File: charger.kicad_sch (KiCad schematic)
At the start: 5 parts, among them J1 Barrel_Jack_Switch, U2 DSIC08LSGET_C3293158

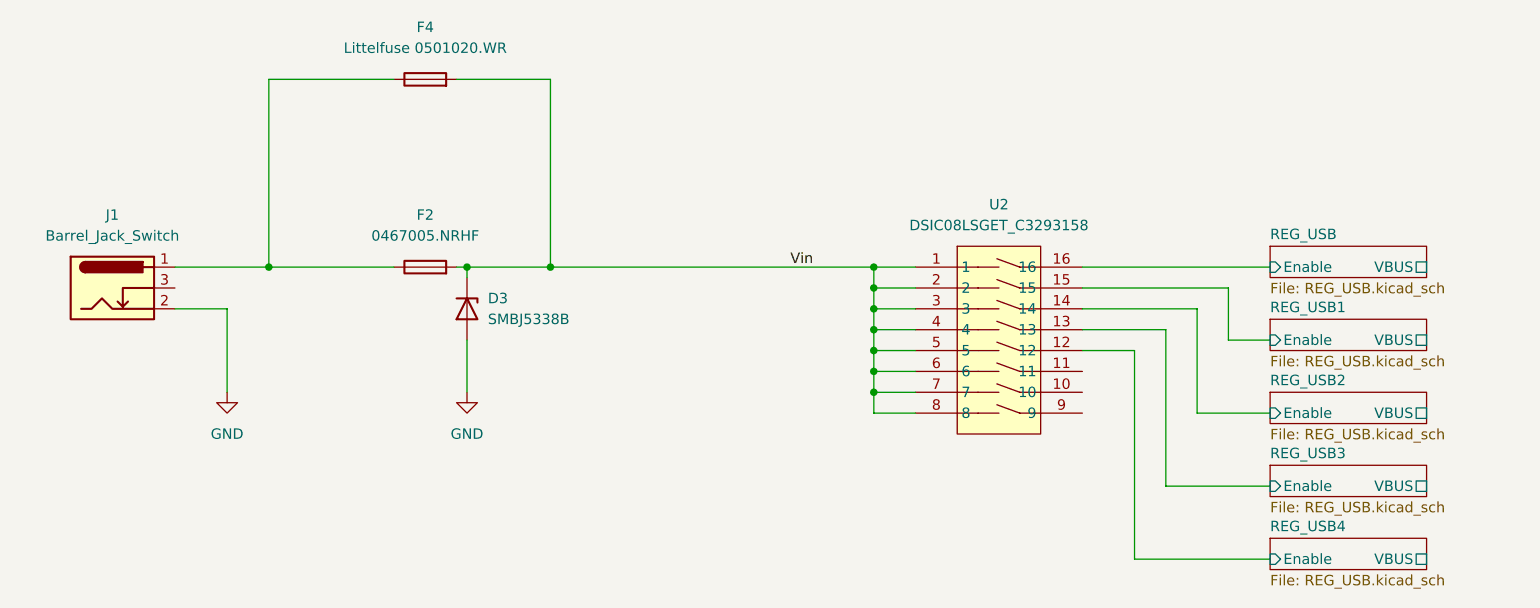
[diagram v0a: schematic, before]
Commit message: finished getting footprints and started layout
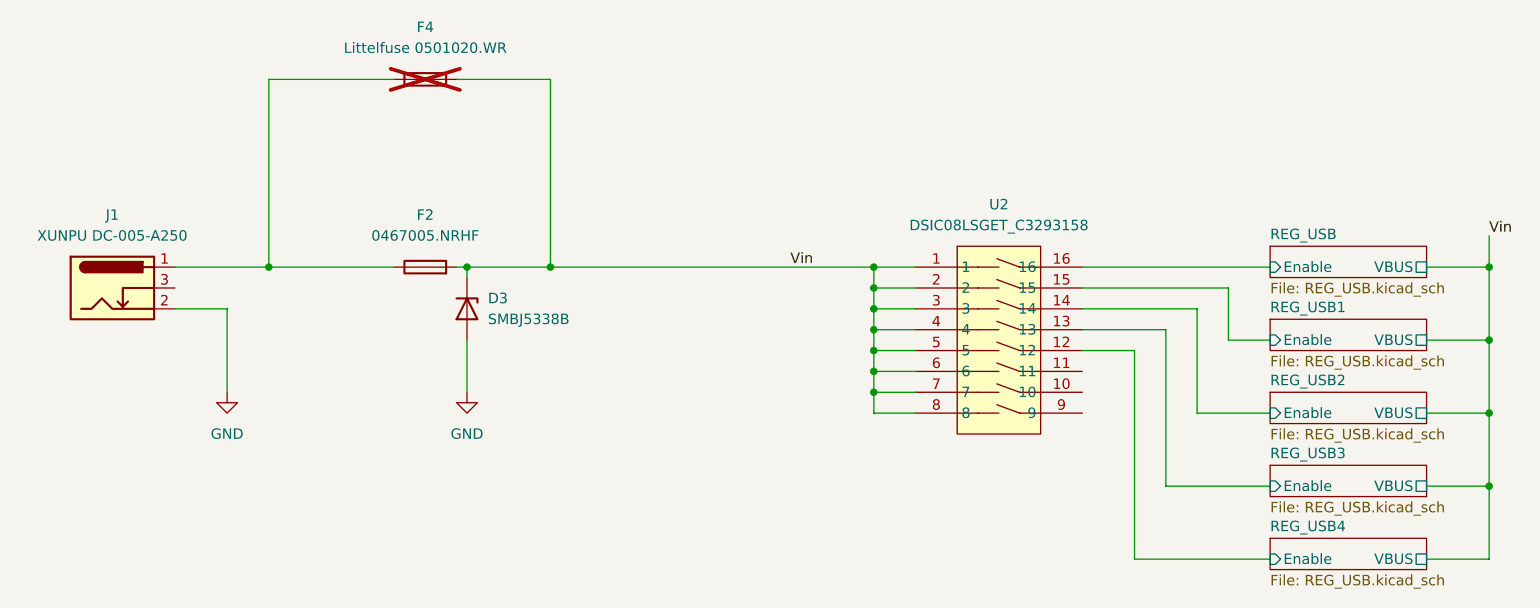
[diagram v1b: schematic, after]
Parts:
- F4: now not fitted
- J1: value Barrel_Jack_Switch -> XUNPU DC-005-A250; footprint (none) -> easyeda2kicad:DC-IN-TH_DC-005-A250
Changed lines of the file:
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@@
+	)
+	(junction
+		(at 204.47 83.82)
+		(diameter 0)
+		(color 0 0 0 0)
 	)
 	(junction
@@
 	)
 	(junction
+		(at 204.47 66.04)
+		(diameter 0)
+		(color 0 0 0 0)
+	)
+	(junction
+		(at 204.47 92.71)
+		(diameter 0)
+		(color 0 0 0 0)
+	)
+	(junction
+		(at 204.47 74.93)
+		(diameter 0)
+		(color 0 0 0 0)
+	)
+	(junction
 		(at 90.17 66.04)
 		(diameter 0)
@@
 	(wire
 		(pts
+			(xy 204.47 66.04) (xy 204.47 74.93)
+		)
+		(stroke
+			(width 0)
+			(type default)
+		)
+	)
+	(wire
+		(pts
 			(xy 44.45 71.12) (xy 50.8 71.12)
 		)
@@
 	(wire
 		(pts
+			(xy 204.47 83.82) (xy 204.47 92.71)
+		)
+		(stroke
+			(width 0)
+			(type default)
+		)
+	)
+	(wire
+		(pts
 			(xy 129.54 71.12) (xy 129.54 68.58)
 		)
@@
 	(wire
 		(pts
+			(xy 204.47 74.93) (xy 204.47 83.82)
+		)
+		(stroke
+			(width 0)
+			(type default)
+		)
+	)
+	(wire
+		(pts
 			(xy 129.54 68.58) (xy 134.62 68.58)
 		)
@@
 	(wire
 		(pts
+			(xy 196.85 83.82) (xy 204.47 83.82)
+		)
+		(stroke
+			(width 0)
+			(type default)
+		)
+	)
+	(wire
+		(pts
 			(xy 44.45 66.04) (xy 55.88 66.04)
 		)
@@
 	(wire
 		(pts
+			(xy 204.47 62.23) (xy 204.47 66.04)
+		)
+		(stroke
+			(width 0)
+			(type default)
+		)
+	)
+	(wire
+		(pts
 			(xy 80.01 66.04) (xy 80.01 67.31)
 		)
@@
 	(wire
 		(pts
+			(xy 196.85 92.71) (xy 204.47 92.71)
+		)
+		(stroke
+			(width 0)
+			(type default)
+		)
+	)
+	(wire
+		(pts
 			(xy 161.29 101.6) (xy 177.8 101.6)
 		)
@@
 	(wire
 		(pts
+			(xy 196.85 74.93) (xy 204.47 74.93)
+		)
+		(stroke
+			(width 0)
+			(type default)
+		)
+	)
+	(wire
+		(pts
 			(xy 129.54 66.04) (xy 134.62 66.04)
 		)
@@
 	(wire
 		(pts
+			(xy 204.47 92.71) (xy 204.47 101.6)
+		)
+		(stroke
+			(width 0)
+			(type default)
+		)
+	)
+	(wire
+		(pts
 			(xy 80.01 66.04) (xy 90.17 66.04)
 		)
@@
 	(wire
 		(pts
+			(xy 196.85 101.6) (xy 204.47 101.6)
+		)
+		(stroke
+			(width 0)
+			(type default)
+		)
+	)
+	(wire
+		(pts
 			(xy 129.54 76.2) (xy 134.62 76.2)
+		)
+		(stroke
+			(width 0)
+			(type default)
+		)
+	)
+	(wire
+		(pts
+			(xy 204.47 66.04) (xy 196.85 66.04)
 		)
 		(stroke
@@
 	(label "Vin"
 		(at 119.38 66.04 0)
+		(effects
+			(font
+				(size 1.27 1.27)
+			)
+			(justify left bottom)
+		)
+	)
+	(label "Vin"
+		(at 204.47 62.23 0)
 		(effects
 			(font
@@
 		(in_bom yes)
 		(on_board yes)
-		(dnp no)
+		(dnp yes)
 		(fields_autoplaced yes)
 		(property "Reference" "F4"
@@
 			)
 		)
-		(property "Value" "Barrel_Jack_Switch"
+		(property "Value" "XUNPU DC-005-A250"
 			(at 36.83 62.23 0)
 			(effects
@@
 			)
 		)
-		(property "Footprint" ""
+		(property "Footprint" "easyeda2kicad:DC-IN-TH_DC-005-A250"
 			(at 38.1 69.596 0)
 			(effects
